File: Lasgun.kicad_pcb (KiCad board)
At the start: 2 copper layers, 15 parts, among them IC1 ATMEGA328P-A, M1 STM32F042G6, M2 EPSON_FA-20H_CRYSTAL, Q1 Q_NMOS_GSD, U1 74LS08

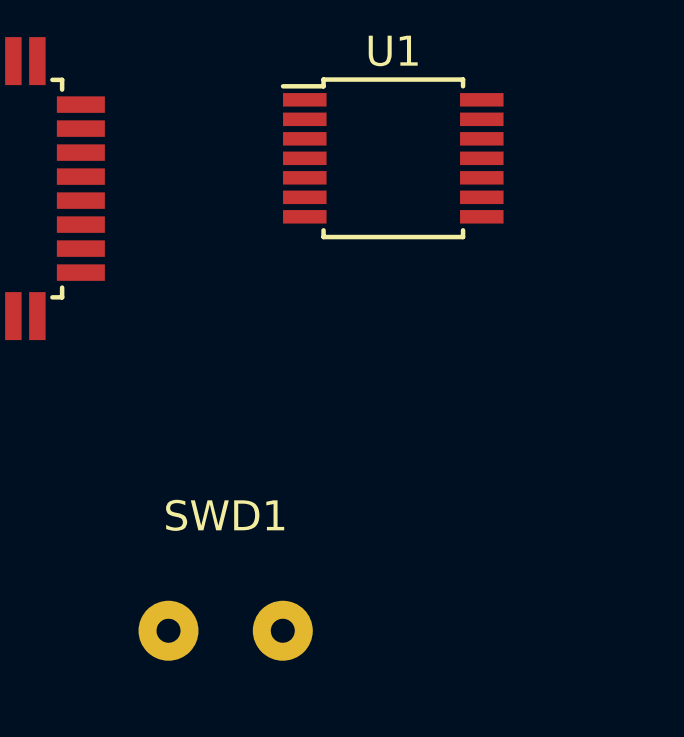
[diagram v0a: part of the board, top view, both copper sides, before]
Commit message: Added IR receiver, tried to tidy up Kicad libs
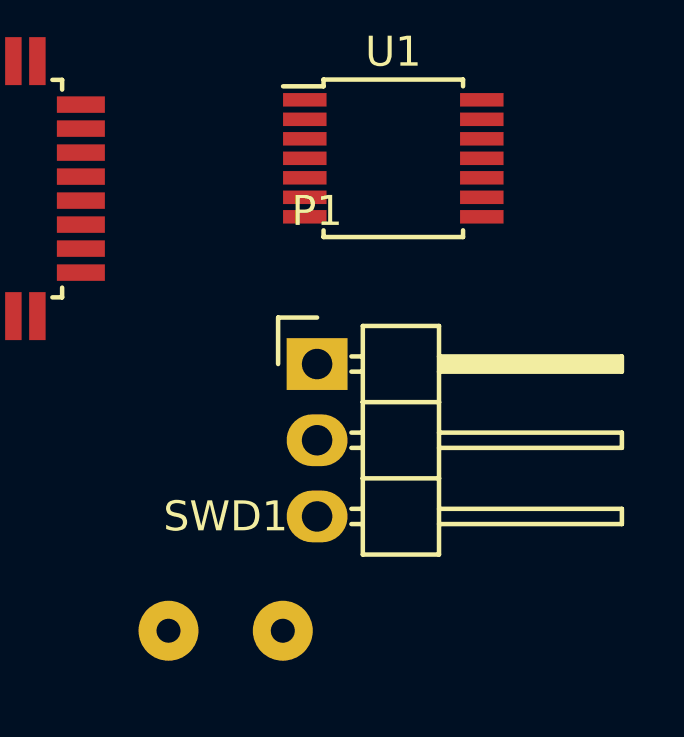
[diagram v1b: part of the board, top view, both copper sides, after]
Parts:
- added P1: CONN_01X03, Pin_Headers:Pin_Header_Angled_1x03, F.Cu at (190.0, 107.7)
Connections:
- IC1 pad 32: (no net) -> IR_RECEIVER1
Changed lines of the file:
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@@
 (kicad_pcb (version 4) (host pcbnew "(2015-05-28 BZR 5690)-product")
   (general
-    (links 34)
-    (no_connects 34)
+    (links 37)
+    (no_connects 37)
     (area 0 0 0 0)
     (thickness 1.6)
@@
     (tracks 0)
     (zones 0)
-    (modules 15)
-    (nets 11)
+    (modules 16)
+    (nets 12)
   )
   (page A4)
@@
   (net 9 "Net-(C5-Pad1)")
   (net 10 "Net-(D1-Pad1)")
+  (net 11 IR_RECEIVER1)
   (net_class Default "This is the default net class."
     (clearance 0.2)
@@
     (add_net +3V3)
     (add_net GND)
+    (add_net IR_RECEIVER1)
     (add_net LED_FET)
     (add_net "Net-(C4-Pad1)")
@@
     (pad 30 smd rect (at -1.2 -4.25 90) (size 1.6 0.55) (layers F.Cu F.Paste F.Mask))
     (pad 31 smd rect (at -2 -4.25 90) (size 1.6 0.55) (layers F.Cu F.Paste F.Mask))
-    (pad 32 smd rect (at -2.8 -4.25 90) (size 1.6 0.55) (layers F.Cu F.Paste F.Mask))
+    (pad 32 smd rect (at -2.8 -4.25 90) (size 1.6 0.55) (layers F.Cu F.Paste F.Mask)
+      (net 11 IR_RECEIVER1))
     (model Housings_QFP.3dshapes/TQFP-32_7x7mm_Pitch0.8mm.wrl
       (at (xyz 0 0 0))
@@
     )
   )
+  (module Pin_Headers:Pin_Header_Angled_1x03 (layer F.Cu)
+    (at 189.992 107.696)
+    (descr "Through hole pin header")
+    (tags "pin header")
+    (fp_text reference P1 (at 0 -5.1) (layer F.SilkS)
+      (effects (font (size 1 1) (thickness 0.15)))
+    )
+    (fp_text value CONN_01X03 (at 0 -3.1) (layer F.Fab)
+      (effects (font (size 1 1) (thickness 0.15)))
+    )
+    (fp_line (start -1.5 -1.75) (end -1.5 6.85) (layer F.CrtYd) (width 0.05))
+    (fp_line (start 10.65 -1.75) (end 10.65 6.85) (layer F.CrtYd) (width 0.05))
+    (fp_line (start -1.5 -1.75) (end 10.65 -1.75) (layer F.CrtYd) (width 0.05))
+    (fp_line (start -1.5 6.85) (end 10.65 6.85) (layer F.CrtYd) (width 0.05))
+    (fp_line (start -1.3 -1.55) (end -1.3 0) (layer F.SilkS) (width 0.15))
+    (fp_line (start 0 -1.55) (end -1.3 -1.55) (layer F.SilkS) (width 0.15))
+    (fp_line (start 4.191 -0.127) (end 10.033 -0.127) (layer F.SilkS) (width 0.15))
+    (fp_line (start 10.033 -0.127) (end 10.033 0.127) (layer F.SilkS) (width 0.15))
+    (fp_line (start 10.033 0.127) (end 4.191 0.127) (layer F.SilkS) (width 0.15))
+    (fp_line (start 4.191 0.127) (end 4.191 0) (layer F.SilkS) (width 0.15))
+    (fp_line (start 4.191 0) (end 10.033 0) (layer F.SilkS) (width 0.15))
+    (fp_line (start 1.524 -0.254) (end 1.143 -0.254) (layer F.SilkS) (width 0.15))
+    (fp_line (start 1.524 0.254) (end 1.143 0.254) (layer F.SilkS) (width 0.15))
+    (fp_line (start 1.524 2.286) (end 1.143 2.286) (layer F.SilkS) (width 0.15))
+    (fp_line (start 1.524 2.794) (end 1.143 2.794) (layer F.SilkS) (width 0.15))
+    (fp_line (start 1.524 4.826) (end 1.143 4.826) (layer F.SilkS) (width 0.15))
+    (fp_line (start 1.524 5.334) (end 1.143 5.334) (layer F.SilkS) (width 0.15))
+    (fp_line (start 4.064 1.27) (end 4.064 -1.27) (layer F.SilkS) (width 0.15))
+    (fp_line (start 10.16 0.254) (end 4.064 0.254) (layer F.SilkS) (width 0.15))
+    (fp_line (start 10.16 -0.254) (end 10.16 0.254) (layer F.SilkS) (width 0.15))
+    (fp_line (start 4.064 -0.254) (end 10.16 -0.254) (layer F.SilkS) (width 0.15))
+    (fp_line (start 1.524 1.27) (end 4.064 1.27) (layer F.SilkS) (width 0.15))
+    (fp_line (start 1.524 -1.27) (end 1.524 1.27) (layer F.SilkS) (width 0.15))
+    (fp_line (start 1.524 -1.27) (end 4.064 -1.27) (layer F.SilkS) (width 0.15))
+    (fp_line (start 1.524 3.81) (end 4.064 3.81) (layer F.SilkS) (width 0.15))
+    (fp_line (start 1.524 3.81) (end 1.524 6.35) (layer F.SilkS) (width 0.15))
+    (fp_line (start 4.064 4.826) (end 10.16 4.826) (layer F.SilkS) (width 0.15))
+    (fp_line (start 10.16 4.826) (end 10.16 5.334) (layer F.SilkS) (width 0.15))
+    (fp_line (start 10.16 5.334) (end 4.064 5.334) (layer F.SilkS) (width 0.15))
+    (fp_line (start 4.064 6.35) (end 4.064 3.81) (layer F.SilkS) (width 0.15))
+    (fp_line (start 4.064 3.81) (end 4.064 1.27) (layer F.SilkS) (width 0.15))
+    (fp_line (start 10.16 2.794) (end 4.064 2.794) (layer F.SilkS) (width 0.15))
+    (fp_line (start 10.16 2.286) (end 10.16 2.794) (layer F.SilkS) (width 0.15))
+    (fp_line (start 4.064 2.286) (end 10.16 2.286) (layer F.SilkS) (width 0.15))
+    (fp_line (start 1.524 3.81) (end 4.064 3.81) (layer F.SilkS) (width 0.15))
+    (fp_line (start 1.524 1.27) (end 1.524 3.81) (layer F.SilkS) (width 0.15))
+    (fp_line (start 1.524 1.27) (end 4.064 1.27) (layer F.SilkS) (width 0.15))
+    (fp_line (start 1.524 6.35) (end 4.064 6.35) (layer F.SilkS) (width 0.15))
+    (pad 1 thru_hole rect (at 0 0) (size 2.032 1.7272) (drill 1.016) (layers *.Cu *.Mask F.SilkS)
+      (net 11 IR_RECEIVER1))
+    (pad 2 thru_hole oval (at 0 2.54) (size 2.032 1.7272) (drill 1.016) (layers *.Cu *.Mask F.SilkS)
+      (net 1 GND))
+    (pad 3 thru_hole oval (at 0 5.08) (size 2.032 1.7272) (drill 1.016) (layers *.Cu *.Mask F.SilkS)
+      (net 2 +3V3))
+    (model Pin_Headers.3dshapes/Pin_Header_Angled_1x03.wrl
+      (at (xyz 0 -0.1 0))
+      (scale (xyz 1 1 1))
+      (rotate (xyz 0 0 90))
+    )
+  )

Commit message: Refined design, added parts, started to plan board
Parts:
- removed C4, C5: C, Capacitors_SMD:C_0603
- removed U1: 74LS08, Housings_SSOP:TSSOP-14_4.4x5mm_Pitch0.65mm
- added BATSIG1: BAT_SIG, Pin_Headers:Pin_Header_Straight_1x02, F.Cu at (130.0, 74.0)
- added CON1: AVR-ISP-6, Pin_Headers:Pin_Header_Straight_2x03, F.Cu at (120.0, 77.0)
- added D2: LED, LEDs:LED-5MM, F.Cu at (157.0, 86.5)
- added P2: CONN_01X03, Pin_Headers:Pin_Header_Angled_1x03, F.Cu at (113.0, 95.5)
- added POW1: R, Resistors_SMD:R_2010_HandSoldering, F.Cu at (148.0, 79.0)
- added POW2: R, Resistors_SMD:R_2010_HandSoldering, F.Cu at (148.0, 74.0)
- added R4: 10K, Resistors_SMD:R_0603, F.Cu at (147.2, 84.2)
- added R5: 1k, Resistors_SMD:R_0603, F.Cu at (145.8, 82.0)
- added R6: 100, Resistors_SMD:R_0603, F.Cu at (147.0, 90.0)
- added cy1: 8pf, Capacitors_SMD:C_0603, F.Cu at (126.0, 94.0)
- added cy2: 8pf, Capacitors_SMD:C_0603, F.Cu at (126.0, 87.0)
- C1, C2, C3: value C -> 100nf
- R1, R2: value R -> 10k
- SWD1: footprint Wire_Pads:SolderWirePad_2x_0-8mmDrill -> Pin_Headers:Pin_Header_Angled_1x02
- moved P1 83.1 mm to (112.0, 79.0), turned to 180 degrees
- moved SWD1 81.1 mm to (112.0, 85.5), turned to 180 degrees
- moved M1 71.0 mm to (119.0, 87.0)
- moved R1 64.7 mm to (116.0, 92.0), turned to 270 degrees
- moved M2 51.7 mm to (126.0, 90.0), turned to 90 degrees
- moved IC1 45.7 mm to (134.0, 89.0)
- moved R3 44.4 mm to (133.0, 82.0)
- moved Q1 39.8 mm to (151.0, 83.3), turned to 270 degrees
- moved R2 36.3 mm to (121.0, 93.0)
- moved C3 31.8 mm to (120.0, 82.0)
- moved C2 28.4 mm to (126.0, 85.0), turned to 180 degrees
- moved D1 28.3 mm to (157.0, 79.0), turned to 90 degrees
- moved C1 18.7 mm to (142.0, 89.0), turned to 90 degrees
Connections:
- D1 pad 2: +3V3 -> Net-(D1-Pad2)
- IC1 pad 12: (no net) -> INPUT_CAPTURE
- IC1 pad 15: (no net) -> AVR_PROG_MOSI
- IC1 pad 16: (no net) -> AVR_PROG_MISO
- IC1 pad 17: (no net) -> AVR_PROG_SCK
- IC1 pad 19: (no net) -> BAT_MON
- IC1 pad 29: !RESET -> ~RESET
- IC1 pad 30: (no net) -> MICRO_RXIN
- IC1 pad 31: (no net) -> MICRO_TXOUT
- M1 pad 19: (no net) -> AVR_PROG_MISO
- M1 pad 20: swdclk -> AVR_PROG_SCK
- M1 pad 4: Net-(M1-Pad4) -> ~RESET
- M1 pad 6: (no net) -> BAT_MON
- M1 pad 7: (no net) -> INPUT_CAPTURE
- M1 pad 8: (no net) -> MICRO_TXOUT
- M1 pad 9: (no net) -> MICRO_RXIN
- Q1 pad 1: LED_FET -> Net-(Q1-Pad1)
- R2 pad 1: Net-(M1-Pad4) -> BAT_MON
- R2 pad 2: +3V3 -> +BATT
- R3 pad 2: !RESET -> ~RESET
- SWD1 pad 1: swdclk -> (no net)
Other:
- board outline added: 50 x 25 mm

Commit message: routing
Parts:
- removed M2: EPSON_FA-20H_CRYSTAL, Ava:Ava-EPSON-FA-20H-CRYSTAL
- removed SWD1: CON_HEADER_1X02-PTH, Pin_Headers:Pin_Header_Angled_1x02
- removed cy1, cy2: 8pf, Capacitors_SMD:C_0603
- added D3: LED, LEDs:LED-3MM, F.Cu at (155.5, 94.5)
- added VREG1: VREG_3PINS-SOT-223, dp_devices:dp_devices-SOT-23, F.Cu at (132.8, 77.5)
- added regc1: 10uf, Capacitors_SMD:C_1206, F.Cu at (140.0, 79.0)
- BATSIG1: footprint Pin_Headers:Pin_Header_Straight_1x02 -> Socket_Strips:Socket_Strip_Angled_1x03
- C1, C2, C3: footprint Capacitors_SMD:C_0603 -> Capacitors_SMD:C_0603_HandSoldering
- R1, R2, R3, R4, R5, R6: footprint Resistors_SMD:R_0603 -> Resistors_SMD:R_0603_HandSoldering
- moved CON1 33.3 mm to (148.5, 94.3), turned to 180 degrees
- moved R2 18.6 mm to (135.2, 81.0), turned to 90 degrees
- moved R5 8.56 mm to (137.2, 81.0), turned to 270 degrees
- moved R6 7.02 mm to (146.5, 83.0), turned to 180 degrees
- moved BATSIG1 6.52 mm to (136.5, 73.5), turned to 180 degrees
- moved R3 5.64 mm to (127.5, 80.8), turned to 270 degrees
- moved C2 4.51 mm to (125.8, 89.5), turned to 270 degrees
- moved R4 2.50 mm to (148.8, 86.2), turned to 0 degrees
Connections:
- BATSIG1 pad 2: +3V3 -> +BATT
- IC1 pad 1: (no net) -> IR_RECEIVER2
- IC1 pad 7: Net-(IC1-Pad7) -> (no net)
- IC1 pad 8: Net-(IC1-Pad8) -> (no net)
- P2 pad 1: (no net) -> IR_RECEIVER2
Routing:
- net +3V3: track 0.00 -> 91.9 mm, vias 0 -> 4
- net ~RESET: track 0.00 -> 49.1 mm, vias 0 -> 4
- net LED_FET: track 0.00 -> 45.5 mm, vias 0 -> 4
- net INPUT_CAPTURE: track 0.00 -> 43.4 mm, vias 0 -> 4
- net AVR_PROG_MISO: track 0.00 -> 42.2 mm, vias 0 -> 2
- net AVR_PROG_SCK: track 0.00 -> 39.4 mm, vias 0 -> 2
- net GND: track 0.00 -> 30.8 mm, vias 0 -> 4
- net IR_RECEIVER1: track 0.00 -> 26.4 mm, vias 0 -> 2
- net +BATT: track 0.00 -> 23.6 mm
- net IR_RECEIVER2: track 0.00 -> 22.4 mm
- net Net-(D1-Pad2): track 0.00 -> 20.1 mm
- net MICRO_RXIN: track 0.00 -> 16.3 mm
- net BAT_MON: track 0.00 -> 16.0 mm, vias 0 -> 2
- net MICRO_TXOUT: track 0.00 -> 16.0 mm, vias 0 -> 2
- net AVR_PROG_MOSI: track 0.00 -> 13.9 mm, vias 0 -> 1
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- added copper zone on B.Cu, net GND
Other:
- net class LEDPower added: clearance 0.2, trace_width 3, via_dia 0.6, via_drill 0.4
